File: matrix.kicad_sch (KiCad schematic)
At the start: 134 parts, among them SW1 esc, SW10 9, SW11 0, SW12 -, SW13 =, SW14 backspace, SW15 del, SW16 tab, SW17 q, SW18 w, SW19 e, SW2 1, SW20 r, SW21 t, SW22 y, SW23 u, SW24 i, SW25 o, SW26 p, SW27 [, SW28 ], SW29 \, SW3 2, SW30 pgup, SW31 capslock, SW32 a, SW33 s, SW34 d, SW35 f, SW36 g, SW37 h, SW38 j, SW39 k, SW4 3, SW40 l, SW41 ;, SW42 ', SW43 enter, SW44 pgdn, SW45 lshift, SW46 z, SW47 x, SW48 c, SW49 v, SW5 4, SW50 b, SW51 n, SW52 m, SW53 ,, SW54 ., SW55 /, SW56 rshift, SW57 up, SW58 fn, SW59 lctrl, SW6 5, SW60 lgui, SW61 lalt, SW63 space, SW64 ralt, SW65 menu, SW66 left, SW67 down, SW68 right, SW7 6, SW8 7, SW9 8

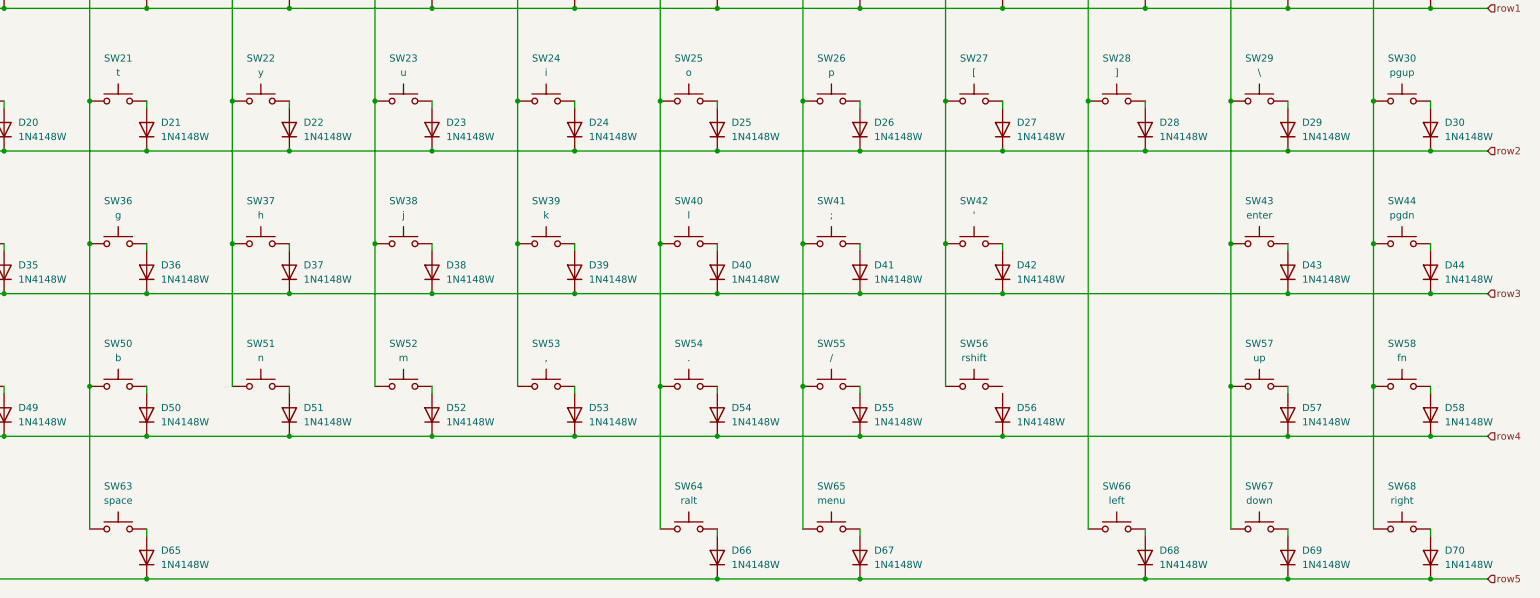
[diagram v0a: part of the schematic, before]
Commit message: add rmk-ble-keyboard %65
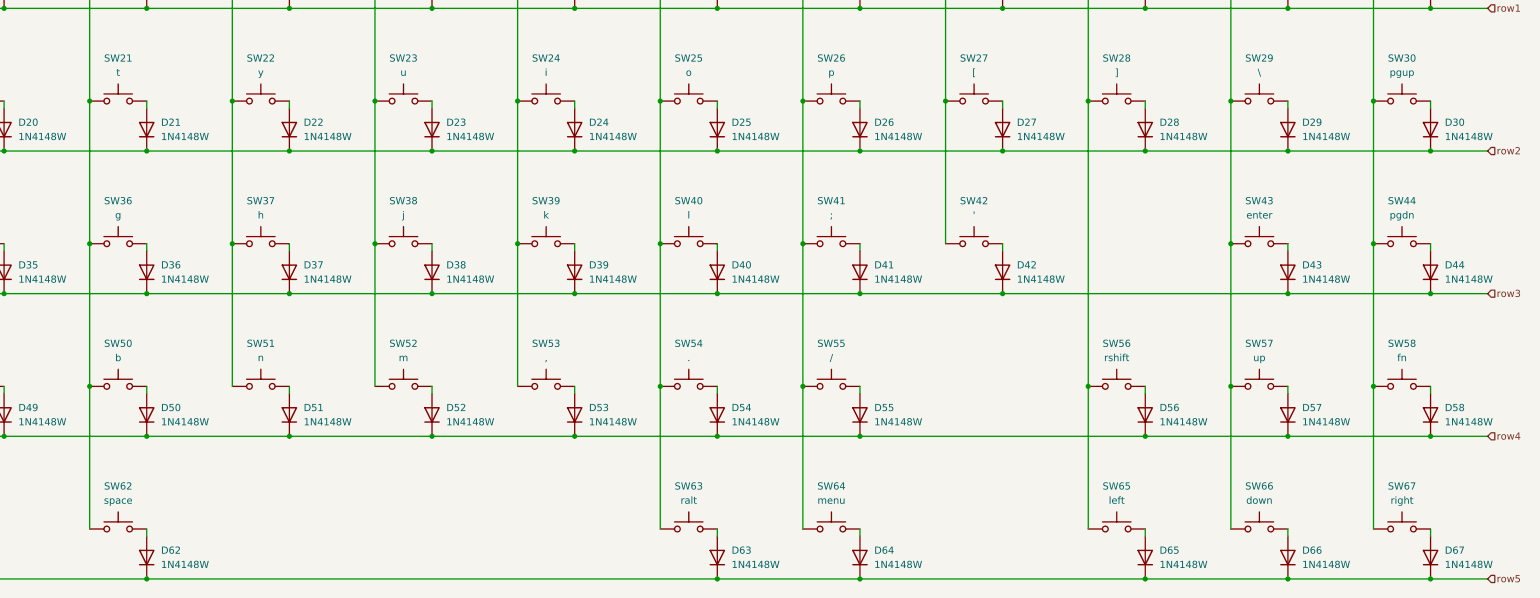
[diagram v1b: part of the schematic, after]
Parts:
- SW15: footprint PCM_Switch_Keyboard_Hotswap_Kailh:SW_Hotswap_Kailh_MX_Plated_2.00u -> PCM_Switch_Keyboard_Hotswap_Kailh:SW_Hotswap_Kailh_MX_Plated_1.00u
- SW30: footprint PCM_Switch_Keyboard_Hotswap_Kailh:SW_Hotswap_Kailh_MX_Plated_1.50u -> PCM_Switch_Keyboard_Hotswap_Kailh:SW_Hotswap_Kailh_MX_Plated_1.00u
- SW44: footprint PCM_Switch_Keyboard_Hotswap_Kailh:SW_Hotswap_Kailh_MX_Plated_2.25u -> PCM_Switch_Keyboard_Hotswap_Kailh:SW_Hotswap_Kailh_MX_Plated_1.00u
- SW56: footprint PCM_Switch_Keyboard_Hotswap_Kailh:SW_Hotswap_Kailh_MX_Plated_2.75u -> PCM_Switch_Keyboard_Hotswap_Kailh:SW_Hotswap_Kailh_MX_Plated_1.75u
- SW57, SW58: footprint PCM_Switch_Keyboard_Hotswap_Kailh:SW_Hotswap_Kailh_MX_Plated_2.75u -> PCM_Switch_Keyboard_Hotswap_Kailh:SW_Hotswap_Kailh_MX_Plated_1.00u
- SW65: renamed from SW66; footprint PCM_Switch_Keyboard_Hotswap_Kailh:SW_Hotswap_Kailh_MX_Plated_1.25u -> PCM_Switch_Keyboard_Hotswap_Kailh:SW_Hotswap_Kailh_MX_Plated_1.00u
- SW66: renamed from SW67; footprint PCM_Switch_Keyboard_Hotswap_Kailh:SW_Hotswap_Kailh_MX_Plated_1.25u -> PCM_Switch_Keyboard_Hotswap_Kailh:SW_Hotswap_Kailh_MX_Plated_1.00u
- SW67: renamed from SW68; footprint PCM_Switch_Keyboard_Hotswap_Kailh:SW_Hotswap_Kailh_MX_Plated_1.25u -> PCM_Switch_Keyboard_Hotswap_Kailh:SW_Hotswap_Kailh_MX_Plated_1.00u
- renumbered D65 to D62, D66 to D63, D67 to D64, D68 to D65, D69 to D66, D70 to D67, SW63 to SW62, SW64 to SW63, SW65 to SW64
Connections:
- net col12: no longer SW56.1
- net col13: now also SW56.1
- net at SW56.2: now also D56.2 (A)
